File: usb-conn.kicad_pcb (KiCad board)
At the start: 2 copper layers, 25 x 12 mm, 8 parts, among them J1 Conn_01x04_Pin, J2 Conn_01x04_Pin, J4 Conn_01x04_Pin, J5 Conn_01x06_Pin, P1 USB_C_Plug_USB2.0, U1 SPX3819M5-L-3-3

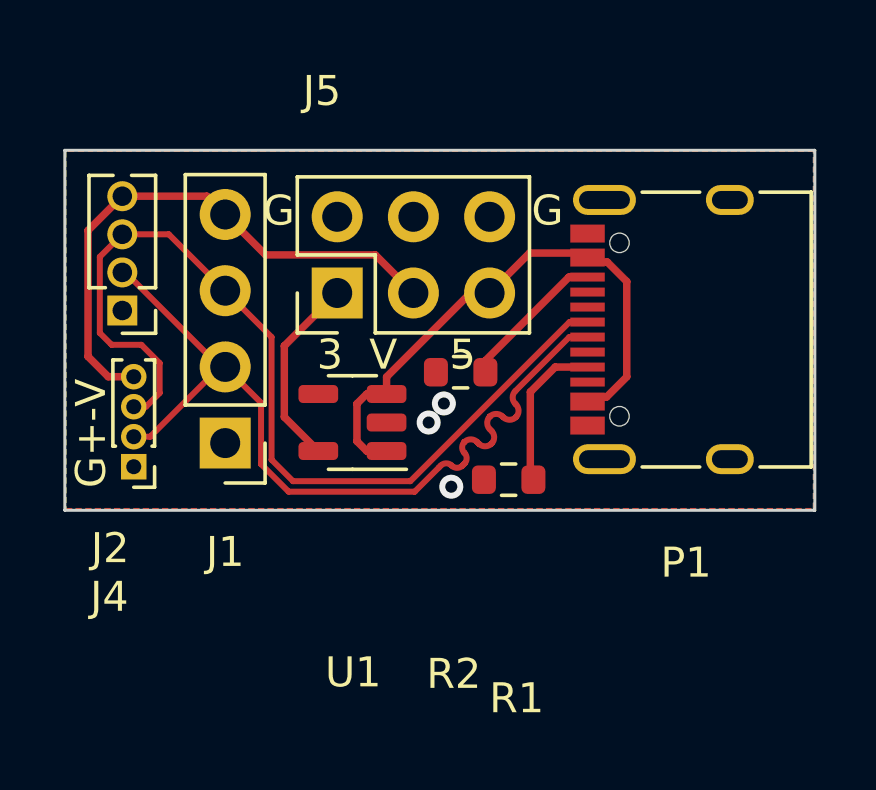
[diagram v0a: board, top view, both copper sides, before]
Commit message: usb-conn: fix connector
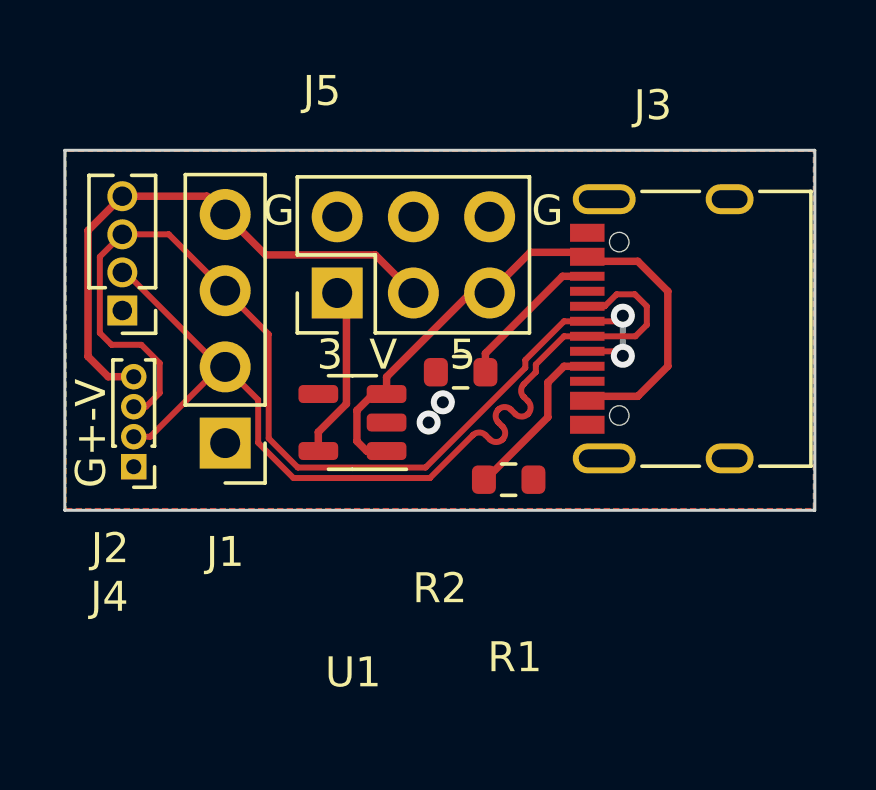
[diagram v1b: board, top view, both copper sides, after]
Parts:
- removed P1: USB_C_Plug_USB2.0, Connector_USB:USB_C_Receptacle_XKB_U262-16XN-4BVC11
- added J3: USB_C_Receptacle_USB2.0_14P, Connector_USB:USB_C_Receptacle_XKB_U262-16XN-4BVC11, F.Cu at (136.1, 81.0)
- R1, R2: value R -> 5.1k
- turned R2 to 0 degrees
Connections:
- R1 pad 1: Net-(P1-CC) -> GND
- R1 pad 2: GND -> Net-(J3-CC1)
- R2 pad 1: Net-(P1-VCONN) -> GND
- R2 pad 2: GND -> Net-(J3-CC2)
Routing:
- net Net-(J3-CC1): track 0.00 -> 5.69 mm
- net Net-(P1-CC): track 5.22 -> 0.00 mm
- net Net-(J3-CC2): track 0.00 -> 5.09 mm
- net Net-(P1-VCONN): track 4.94 -> 0.00 mm
- net /D+: track 27.7 -> 32.3 mm
- net /D-: track 31.6 -> 34.8 mm, vias 0 -> 2
- net /5V: track 18.8 -> 21.0 mm
- net /3V3: track 6.47 -> 5.78 mm
- net GND: vias 3 -> 2

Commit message: usb-conn: layout update
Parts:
- moved R1 2.10 mm to (130.5, 84.0), turned to 90 degrees
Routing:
- net /D-: track 34.8 -> 39.3 mm, vias 2 -> 0
- net Net-(J3-CC1): track 5.69 -> 2.32 mm
- net /D+: track 32.3 -> 35.5 mm
- net GND: vias 2 -> 0
